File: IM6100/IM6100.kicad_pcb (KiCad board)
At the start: 4 copper layers, 180 x 120 mm, 126 parts, among them SW1 SS-12SDP2, SW10 SS-12SDP2, SW11 SS-12SDP2, SW12 SS-12SDP2, SW13 DTSM-63N-V-T/R, SW14 SS-12SDP2, SW15 DTSM-63N-V-T/R, SW16 DTSM-63N-V-T/R, SW17 SS-12SDP2, SW18 DTSM-63N-V-T/R, SW19 ERD216CSZ, SW2 SS-12SDP2, SW20 DTSM-63N-V-T/R, SW3 SS-12SDP2, SW4 SS-12SDP2, SW5 SS-12SDP2, SW6 SS-12SDP2, SW7 SS-12SDP2, SW8 SS-12SDP2, SW9 SS-12SDP2, U1 IM6100, U10 SN74LVC245APW, U11 SN74LVC574APW, U12 SN74LVC574APW, U13 SN74AHC1G04, U2 TXB0108PW, U3 TXB0108PW, U4 TXB0108PW, U5 TXB0108PW, U6 Tang_Nano_9K, U7 SN74LVC574APW, U8 SN74LVC245APW, U9 SN74LVC574APW, Y1 4MHz

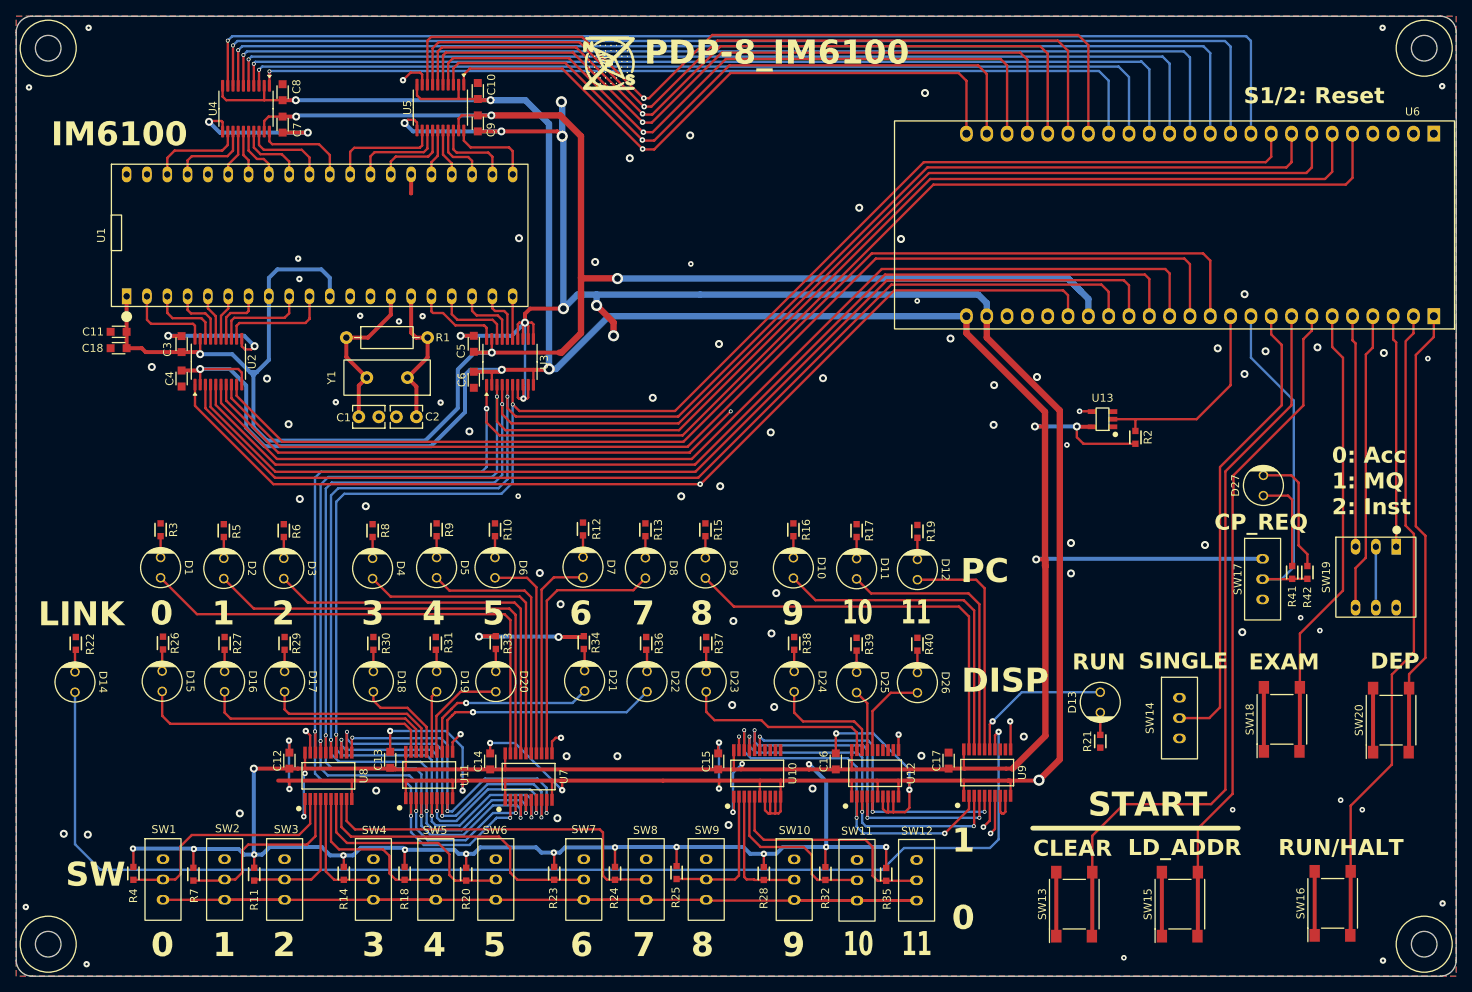
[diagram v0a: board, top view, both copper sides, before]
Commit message: Replaced level shifter logics to SN74LVC8T245.
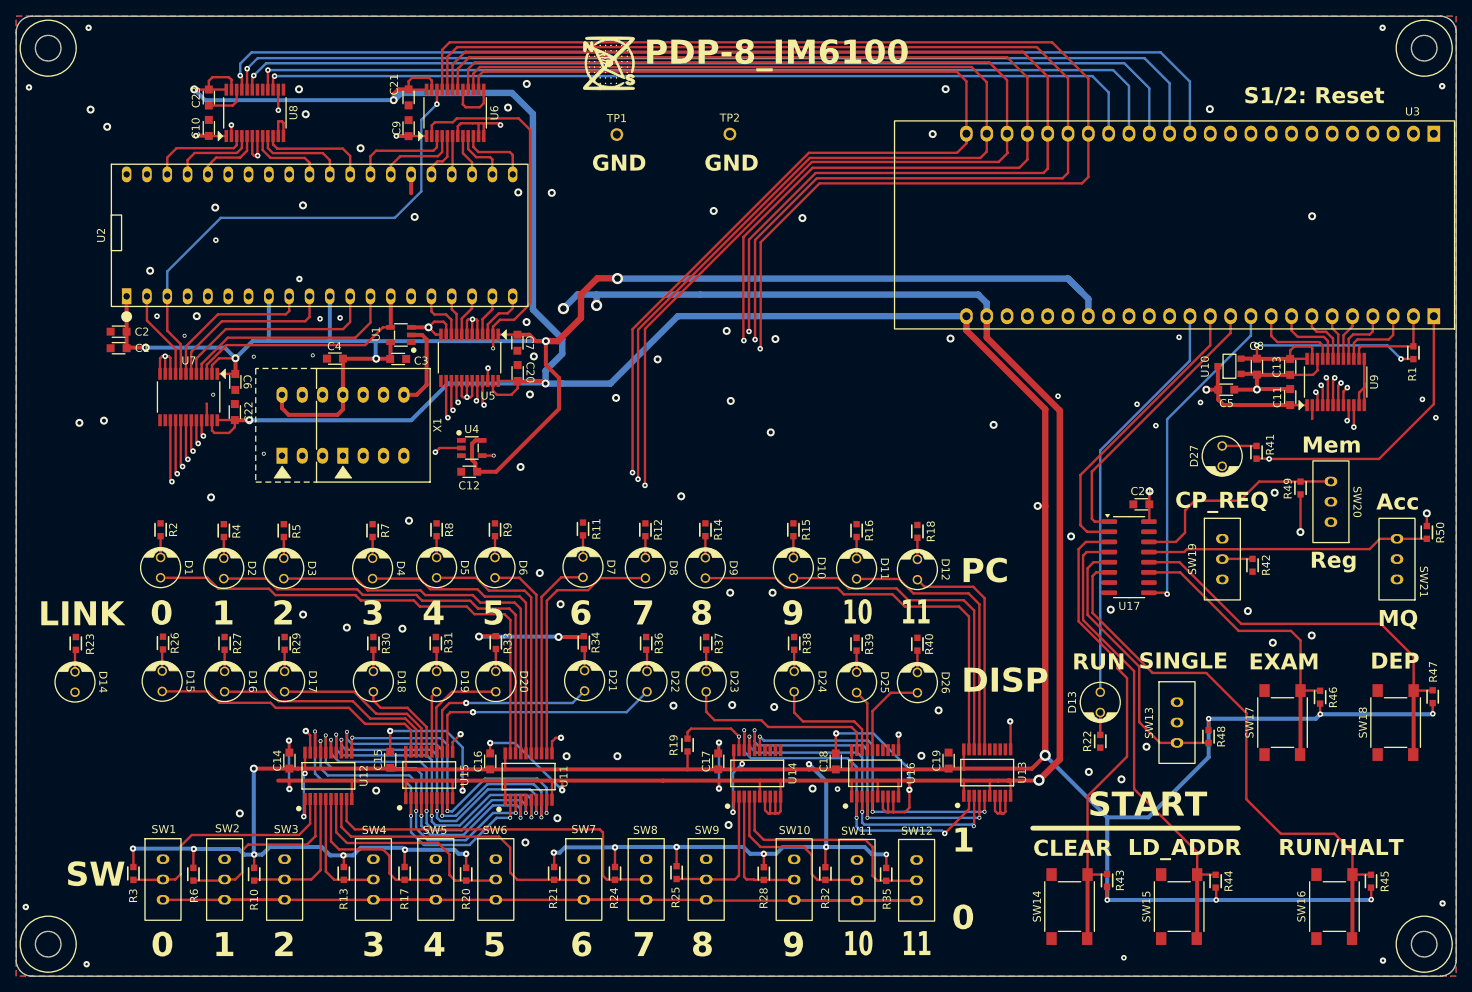
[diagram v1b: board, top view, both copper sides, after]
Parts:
- removed the C1 at (91.5, 80.8)
- removed the C2 at (93.7, 80.8)
- removed the R2 at (186.0, 83.3)
- removed the U13 at (181.9, 81.1)
- removed the U2 at (71.4, 73.9)
- removed the U3 at (107.9, 73.9)
- removed Y1: 4MHz, 0my_project:Y_2P
- added C12: 0.1uF, 0my_project:C_1608_0603, F.Cu at (102.8, 87.7)
- added C13: 0.1uF, 0my_project:C_1608_0603, F.Cu at (205.4, 74.5)
- added C20: 0.1uF, 0my_project:C_1608_0603, F.Cu at (108.8, 75.3)
- added C21: 0.1uF, 0my_project:C_1608_0603, F.Cu at (95.2, 40.9)
- added C22: 0.1uF, 0my_project:C_1608_0603, F.Cu at (73.5, 80.2)
- added C23: 0.1uF, 0my_project:C_1608_0603, F.Cu at (70.2, 40.9)
- added C24: 0.1uF, 0my_project:C_1608_0603, F.Cu at (186.8, 91.7)
- added C5: 1uF, 0my_project:C_1608_0603, F.Cu at (197.4, 77.4)
- added R19: 10K, 0my_project:R_1608_0603, F.Cu at (130.1, 121.8)
- added R43: 10K, 0my_project:R_1608_0603, F.Cu at (182.5, 138.7)
- added R44: 10K, 0my_project:R_1608_0603, F.Cu at (196.1, 138.8)
- added R45: 10K, 0my_project:R_1608_0603, F.Cu at (215.5, 138.8)
- added R46: 10K, 0my_project:R_1608_0603, F.Cu at (209.1, 115.8)
- added R47: 10K, 0my_project:R_1608_0603, F.Cu at (223.2, 115.8)
- added R48: 10K, 0my_project:R_1608_0603, F.Cu at (195.2, 120.8)
- added R49: 10K, 0my_project:R_1608_0603, F.Cu at (206.7, 89.7)
- added R50: 10K, 0my_project:R_1608_0603, F.Cu at (222.5, 95.2)
- added SW21: SS-12SDP2, 0my_project:SS-12SDP2, F.Cu at (218.7, 98.6)
- added TP1: TEST-34, 0my_project:TEST-34, F.Cu at (121.2, 45.5)
- added TP2: TEST-34, 0my_project:TEST-34, F.Cu at (135.3, 45.4)
- added U1: SN74AHCT1G14DBV, 0my_project:SOT-23-5_TI, F.Cu at (94.2, 70.5)
- added U10: AP2127N-1.8, 0my_project:SOT-23_AP2127N, F.Cu at (197.8, 74.5)
- added U17: 74HC165D, Package_SO:SOIC-16_3.9x9.9mm_P1.27mm, F.Cu at (185.3, 98.3)
- added U6: SN74LVC8T245PWR, 0my_project:TSSOP-24_TI-PW, F.Cu at (101.0, 42.8)
- added U7: SN74LVC8T245PWR, 0my_project:TSSOP-24_TI-PW, F.Cu at (67.7, 78.3)
- added U8: SN74LVC8T245PWR, 0my_project:TSSOP-24_TI-PW, F.Cu at (76.0, 42.8)
- added U9: SN74LVC8T245PWR, 0my_project:TSSOP-24_TI-PW, F.Cu at (211.1, 76.4)
- added X1: 4MHz Clock Oscillator, 0my_project:DIP-14_ClockOscillator, F.Cu at (87.0, 81.8)
- C8: value 0.1uF -> 1uF
- R1: value 1M -> 10K; footprint Resistor_THT:R_Axial_DIN0207_L6.3mm_D2.5mm_P10.16mm_Horizontal -> 0my_project:R_1608_0603
- SW13, SW20: value DTSM-63N-V-T/R -> SS-12SDP2; footprint 0my_project:DTSM-6x -> 0my_project:SS-12SDP2
- SW14, SW17: value SS-12SDP2 -> DTSM-63N-V-T/R; footprint 0my_project:SS-12SDP2 -> 0my_project:DTSM-6x
- SW19: value ERD216CSZ -> SS-12SDP2; footprint 0my_project:ERD216CSZ -> 0my_project:SS-12SDP2
- U4: value TXB0108PW -> SN74AHCT1G14DBV; footprint Package_SO:TSSOP-20_4.4x6.5mm_P0.65mm -> 0my_project:SOT-23-5_TI
- U5: value TXB0108PW -> SN74LVC8T245PWR; footprint Package_SO:TSSOP-20_4.4x6.5mm_P0.65mm -> 0my_project:TSSOP-24_TI-PW
- moved C11 146.7 mm to (205.4, 78.3), turned to 90 degrees
- moved R1 133.4 mm to (220.8, 72.8), turned to -90 degrees
- moved C8 126.5 mm to (201.2, 74.5), turned to -90 degrees
- moved U4 50.9 mm to (103.1, 84.7), turned to 0 degrees
- moved C7 40.1 mm to (108.8, 71.5)
- moved C10 33.9 mm to (70.2, 44.7)
- moved U5 31.5 mm to (102.8, 73.4), turned to 180 degrees
- moved C6 29.8 mm to (73.5, 76.4)
- moved SW20 28.3 mm to (210.5, 91.4), turned to 180 degrees
- moved SW14 27.3 mm to (177.8, 142.0), turned to 90 degrees
- moved SW13 26.1 mm to (191.2, 119.0), turned to 0 degrees
- moved C4 19.3 mm to (86.0, 73.5), turned to 180 degrees
- moved SW19 19.3 mm to (196.9, 98.6)
- moved SW17 18.1 mm to (204.4, 119.0), turned to 90 degrees
- moved R41 15.7 mm to (201.2, 85.2)
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- renumbered C18 to C1, C12 to C14, C13 to C15, C14 to C16, C15 to C17, C16 to C18, C17 to C19, C3 to C2, C5 to C3, R11 to R10, R12 to R11, R13 to R12, R14 to R13, R15 to R14, R16 to R15, R17 to R16, R18 to R17, R19 to R18, R3 to R2, R23 to R21, R21 to R22, R22 to R23, R4 to R3, R5 to R4, R6 to R5, R7 to R6, R8 to R7, R9 to R8, R10 to R9, U7 to U11, U8 to U12, U9 to U13, U10 to U14, U11 to U15, U12 to U16, U1 to U2, U6 to U3
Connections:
- C10 pad 1: +3.3V -> +5V
- C4 pad 1: +3.3V -> +5V
- C6 pad 1: +3.3V -> +5V
- C8 pad 1: +3.3V -> +1V8
- D13 pad 2: Net-(D13-A) -> /RUN_3V3
- D14 pad 2: Net-(D14-A) -> /LINK_3V3
- R1 pad 1: Net-(U1-OSC_OUT) -> /~{RESET_3V3}
- R1 pad 2: Net-(U1-OSC_IN) -> +1V8
- SW13 pad 1: GND -> /Tactile Switches/Single_SW
- SW13 pad 3: /CLEAR_SW -> unconnected-(SW13-Pad3)
- SW14 pad 2: /SINGLE_SW -> GND
- SW14 pad 3: unconnected-(SW14-Pad3) -> /Tactile Switches/Clear_SW
- SW15 pad 3: /LD_ADDR_SW -> /Tactile Switches/LoadAd_SW
- SW15 pad 4: /LD_ADDR_SW -> /Tactile Switches/LoadAd_SW
- SW16 pad 3: /CONT_SW -> /Tactile Switches/RunHlt_SW
- SW16 pad 4: /CONT_SW -> /Tactile Switches/RunHlt_SW
- SW17 pad 1: unconnected-(SW17-Pad1) -> GND
- SW17 pad 2: /CPREQ_ON -> GND
- SW17 pad 3: +3.3V -> /Tactile Switches/Exam_SW
- SW18 pad 3: /EXAM_SW -> /Tactile Switches/Dep_SW
- SW18 pad 4: /EXAM_SW -> /Tactile Switches/Dep_SW
- SW19 pad 1: /MODE_SW0 -> unconnected-(SW19-Pad1)
- SW19 pad 2: GND -> /CPREQ_ON
- SW19 pad 3: /MODE_SW2 -> +3.3V
- SW20 pad 1: GND -> /Tactile Switches/MemReg_SW
- SW20 pad 3: /DEP_SW -> unconnected-(SW20-Pad3)
- U13 pad 14: Net-(D14-A) -> unconnected-(U13-Q5-Pad14)
- U13 pad 15: Net-(D13-A) -> unconnected-(U13-Q4-Pad15)
- U13 pad 6: /RUN_3V3 -> GND
- U13 pad 7: /LINK_3V3 -> GND
- U2 pad 12: unconnected-(U1-XTB-Pad12) -> /XTB
- U2 pad 13: unconnected-(U1-XTC-Pad13) -> /XTC
- U2 pad 14: Net-(U1-OSC_OUT) -> Clock
- U2 pad 15: Net-(U1-OSC_IN) -> GND
- U2 pad 36: unconnected-(U1-IFETCH-Pad36) -> /IFETCH
- U3 pad 10: /~{CPSEL_3V3} -> /DX2_3V3
- U3 pad 11: /~{MEMSEL_3V3} -> /DX3_3V3
- U3 pad 12: /~{SKP_3V3} -> /DX4_3V3
- U3 pad 13: /~{C2_3V3} -> /~{CPSEL_3V3}
- U3 pad 14: /~{C1_3V3} -> /~{MEMSEL_3V3}
- U3 pad 15: /~{C0_3V3} -> /IFETCH_3V3
- U3 pad 30: /RUN_3V3 -> unconnected-(U3-48_IOR24B-Pad30)
- U3 pad 32: /DMAGNT_3V3 -> /XTB_3V3
- U3 pad 33: /~{DMAREQ_3V3} -> /LXMAR_3V3
- U3 pad 34: /~{CPREQ_3V3} -> /XTA_3V3
- U3 pad 35: /~{RUN/HLT_3V3} -> /DMAGNT_3V3
- U3 pad 36: /XTA_3V3 -> /RUN_3V3
- U3 pad 37: /LXMAR_3V3 -> /SW_CLK
- U3 pad 38: MK_RESET -> /SW_LATCH
- U3 pad 39: /CPREQ_ON -> /SW_DATA
- U3 pad 40: /SINGLE_SW -> /~{CPREQ_3V3}
- U3 pad 41: /CLEAR_SW -> /~{DMAREQ_3V3}
- U3 pad 42: /LD_ADDR_SW -> /~{SKP_3V3}
- U3 pad 43: /EXAM_SW -> /~{C2_3V3}
- U3 pad 44: /MODE_SW2 -> /~{C1_3V3}
- U3 pad 45: /MODE_SW1 -> /~{C0_3V3}
- U3 pad 46: /MODE_SW0 -> /~{RUN/HLT_3V3}
- U3 pad 47: /CONT_SW -> /~{RESET_3V3}
- U3 pad 48: /DEP_SW -> /CPREQ_ON
- U3 pad 5: /DX0_3V3 -> unconnected-(U3-25_IOB8A-Pad5)
- U3 pad 6: /DX1_3V3 -> /XTC_3V3
- U3 pad 7: /DX2_3V3 -> /CLOCK_3V3
- U3 pad 8: /DX3_3V3 -> /DX0_3V3
- U3 pad 9: /DX4_3V3 -> /DX1_3V3
- U4 pad 1: /~{DEVSEL_3V3} -> unconnected-(U4-NC-Pad1)
- U4 pad 2: +3.3V -> /XTA
- U4 pad 3: /~{SWSEL_3V3} -> GND
- U4 pad 4: /~{C0_3V3} -> ~{DIR_READ}
- U4 pad 5: /~{C1_3V3} -> +5V
- U5 pad 1: /DX5_3V3 -> +5V
- U5 pad 10: +3.3V -> /DX0
- U5 pad 12: /LINK -> GND
- U5 pad 13: /DX11 -> GND
- U5 pad 14: /DX10 -> /DX0_3V3
- U5 pad 15: /DX9 -> /DX1_3V3
- U5 pad 16: /DX8 -> /DX2_3V3
- U5 pad 17: /DX7 -> GND
- U5 pad 18: /DX6 -> GND
- U5 pad 19: +5V -> GND
- U5 pad 2: +3.3V -> ~{DIR_READ}
- U5 pad 20: /DX5 -> /DX3_3V3
- U5 pad 3: /DX6_3V3 -> /DX4
- U5 pad 4: /DX7_3V3 -> /DX3
- U5 pad 5: /DX8_3V3 -> GND
- U5 pad 6: /DX9_3V3 -> GND
- U5 pad 7: /DX10_3V3 -> GND
- U5 pad 8: /DX11_3V3 -> /DX2
- U5 pad 9: /LINK_3V3 -> /DX1
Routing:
- net /XTC_3V3: track 0.00 -> 164.3 mm, vias 0 -> 1
- net /CLOCK_3V3: track 0.00 -> 159.4 mm, vias 0 -> 1
- net /~{SKP}: track 5.87 -> 159.7 mm, vias 0 -> 1
- net /~{C2}: track 5.62 -> 159.0 mm, vias 0 -> 1
- net Net-(D14-A): track 153.2 -> 0.00 mm, vias 1 -> 0
- net /~{RUN/HLT}: track 5.68 -> 156.8 mm, vias 0 -> 1
- net /~{C1}: track 6.90 -> 158.0 mm, vias 0 -> 1
- net /~{DMAREQ}: track 7.56 -> 158.3 mm, vias 0 -> 1
- net /~{C0}: track 8.74 -> 158.0 mm, vias 0 -> 1
- net /~{CPREQ}: track 5.72 -> 153.5 mm, vias 0 -> 1
- net /~{RESET}: track 7.64 -> 154.3 mm, vias 0 -> 1
- net /XTB_3V3: track 0.00 -> 130.8 mm, vias 0 -> 1
- net /~{SKP_3V3}: track 136.6 -> 7.11 mm, vias 1 -> 0
- net /~{RUN/HLT_3V3}: track 139.2 -> 10.1 mm
- net /~{C2_3V3}: track 132.2 -> 5.64 mm, vias 1 -> 0
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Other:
- board text added: "Acc"
- board text added: "DRC Error: 1, warning: 0"
- board text added: "GND"
- board text added: "MQ"
- board text added: "Mem"
- board text added: "Project: PDP-8_IM6100 Rev. 2.0 (2025/11)"
- board text added: "Reg"
- board text removed: "0: Acc 1: MQ 2: Inst"
- board text removed: "DRC Error: 2, warning: 28"
- board text removed: "IM6100"
- board text removed: "Project: PDP-8_IM6100 Rev. 1.0 (2025/09)"
